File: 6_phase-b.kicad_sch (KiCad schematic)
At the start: 28 parts, among them Q401 BSC072N08NS5, Q402 BSC072N08NS5, U401 IR2181S, U402 AD8418

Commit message: feat: LED routing, encoder interface, footprint updates
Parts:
- removed H?: Pad, symbol Mechanical:MountingHole_Pad
- added H?: Pad, symbol Mechanical:MountingHole_Pad
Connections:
- net at R410.4: now also H?.1

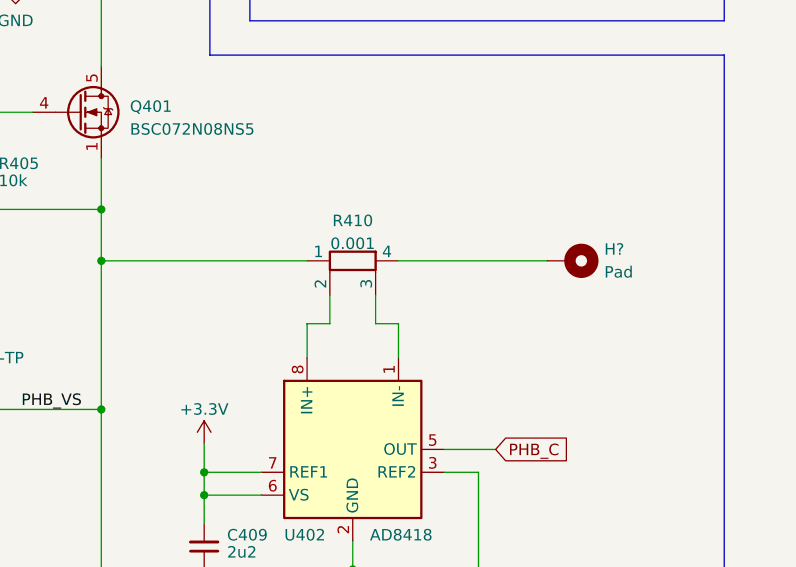
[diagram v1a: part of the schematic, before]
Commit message: feat: footprint assignment, circuit check and routing kickoff
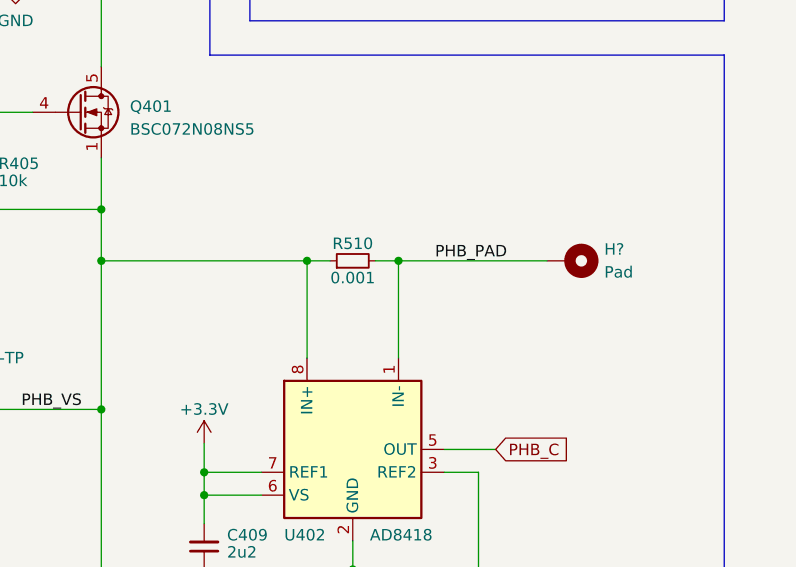
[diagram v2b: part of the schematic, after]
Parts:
- removed R410: 0.001, Resistor_SMD:R_2512_6332Metric, symbol Device:R_Shunt
- added R510: 0.001, Resistor_SMD:R_1206_3216Metric_Pad1.30x1.75mm_HandSolder, symbol Device:R_Small
- C410: footprint Capacitor_SMD:C_0402_1005Metric_Pad0.74x0.62mm_HandSolder -> Capacitor_SMD:C_0603_1608Metric_Pad1.08x0.95mm_HandSolder
- D401: Link (none) -> https://www.digikey.de/en/products/detail/rohm-semiconducto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
- D402: Link (none) -> https://www.digikey.de/en/products/detail/micro-commercial-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
- H?: footprint (none) -> TestPoint:TestPoint_THTPad_4.0x4.0mm_Drill2.0mm
- Q401, Q402: Link (none) -> https://www.digikey.de/en/products/detail/infineon-technolo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
- R408, R409: footprint Resistor_SMD:R_0402_1005Metric_Pad0.72x0.64mm_HandSolder -> Resistor_SMD:R_0603_1608Metric_Pad0.98x0.95mm_HandSolder
- U402: Link (none) -> https://www.digikey.de/en/products/detail/analog-devices-in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
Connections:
- net PHB_VS: now also U402.8 (IN+), R510.1
- net PHB_PAD: now reaches U402.1 (IN-)
- net PHB_PAD: now also H?.1, R510.2
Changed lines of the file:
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@@
   (title_block
     (title "3-Phase Bridge - Phase B")
-    (date "2023-11-25")
+    (date "2023-11-26")
     (rev "1.0")
   )
+  (junction (at 244.475 83.185) (diameter 0) (color 0 0 0 0)
+  )
   (junction (at 189.865 99.695) (diameter 0) (color 0 0 0 0)
   )
@@
   (junction (at 250.19 35.56) (diameter 0) (color 0 0 0 0)
   )
+  (junction (at 234.315 83.185) (diameter 0) (color 0 0 0 0)
+  )
   (junction (at 198.755 66.675) (diameter 0) (color 0 0 0 0)
   )
@@
   (junction (at 201.93 40.005) (diameter 0) (color 0 0 0 0)
   )
-  (wire (pts (xy 236.855 90.17) (xy 236.855 86.995))
-    (stroke (width 0) (type default))
-  )
   (wire (pts (xy 42.545 95.885) (xy 47.625 95.885))
     (stroke (width 0) (type default))
@@
     (stroke (width 0) (type default))
   )
-  (wire (pts (xy 241.935 86.995) (xy 241.935 90.17))
-    (stroke (width 0) (type default))
-  )
   (wire (pts (xy 191.77 48.895) (xy 191.77 52.07))
     (stroke (width 0) (type default))
@@
     (stroke (width 0) (type default))
   )
-  (wire (pts (xy 241.935 90.17) (xy 244.475 90.17))
-    (stroke (width 0) (type default))
-  )
   (wire (pts (xy 77.47 73.66) (xy 77.47 76.2))
     (stroke (width 0) (type default))
   )
-  (wire (pts (xy 234.315 90.17) (xy 236.855 90.17))
-    (stroke (width 0) (type default))
-  )
   (polyline (pts (xy 223.52 60.325) (xy 223.52 20.955))
     (stroke (width 0) (type default))
@@
     (stroke (width 0) (type default))
   )
-  (wire (pts (xy 234.315 93.98) (xy 234.315 90.17))
+  (wire (pts (xy 234.315 83.185) (xy 234.315 93.98))
     (stroke (width 0) (type default))
   )
@@
     (stroke (width 0) (type default))
   )
+  (wire (pts (xy 244.475 83.185) (xy 260.985 83.185))
+    (stroke (width 0) (type default))
+  )
   (wire (pts (xy 229.235 109.22) (xy 222.885 109.22))
     (stroke (width 0) (type default))
@@
     (stroke (width 0) (type default))
   )
+  (wire (pts (xy 234.315 83.185) (xy 236.855 83.185))
+    (stroke (width 0) (type default))
+  )
   (wire (pts (xy 239.395 117.475) (xy 253.365 117.475))
     (stroke (width 0) (type default))
@@
     (stroke (width 0) (type default))
   )
-  (wire (pts (xy 244.475 83.185) (xy 260.985 83.185))
+  (wire (pts (xy 241.935 83.185) (xy 244.475 83.185))
     (stroke (width 0) (type default))
   )
@@
     (stroke (width 0) (type default))
   )
-  (wire (pts (xy 244.475 90.17) (xy 244.475 93.98))
+  (wire (pts (xy 244.475 83.185) (xy 244.475 93.98))
     (stroke (width 0) (type default))
   )
@@
   (label "PHB_HOUT_G" (at 185.42 66.675 0) (fields_autoplaced)
     (effects (font (size 1.27 1.27)) (justify left bottom))
+  )
+  (label "PHB_PAD" (at 256.54 83.185 180) (fields_autoplaced)
+    (effects (font (size 1.27 1.27)) (justify right bottom))
   )
   (label "PHB_HOUT" (at 108.585 85.725 180) (fields_autoplaced)
@@
     (property "Datasheet" "http://www.infineon.com/dgdl/Infineon-BSC072N08NS5-DS-v02_00-EN.pdf?fileId=5546d4624ad04ef9014ae3d8e8192c7c" (at 208.915 66.675 90)
       (effects (font (size 1.27 1.27)) (justify left) hide)
+    )
+    (property "Link" "https://www.digikey.de/en/products/detail/infineon-technologies/BSC072N08NS5ATMA1/5959908" (at 208.915 66.675 0)
+      (effects (font (size 1.27 1.27)) hide)
     )
     (pin "1")
@@
       (effects (font (size 1.27 1.27)) hide)
     )
+    (property "Link" "https://www.digikey.de/en/products/detail/analog-devices-inc/AD8418AWBRZ/4571735" (at 239.395 104.14 0)
+      (effects (font (size 1.27 1.27)) hide)
+    )
     (pin "1")
     (pin "2")
@@
       (effects (font (size 1.27 1.27)) (justify left))
     )
-    (property "Footprint" "Resistor_SMD:R_0402_1005Metric_Pad0.72x0.64mm_HandSolder" (at 184.785 105.41 0)
+    (property "Footprint" "Resistor_SMD:R_0603_1608Metric_Pad0.98x0.95mm_HandSolder" (at 184.785 105.41 0)
       (effects (font (size 1.27 1.27)) hide)
     )
@@
         (path "/9dea2e18-5867-4ed4-a12d-7ee109225de0/912dc4da-f7bc-46bd-8800-06fc31d708dd"
           (reference "#PWR044") (unit 1)
-        )
-      )
-    )
-  )
-  (symbol (lib_id "Device:R_Shunt") (at 239.395 83.185 90) (mirror x) (unit 1)
-    (in_bom yes) (on_board yes) (dnp no)
-    (property "Reference" "R410" (at 239.395 78.74 90)
-      (effects (font (size 1.27 1.27)))
-    )
-    (property "Value" "0.001" (at 239.395 81.28 90)
-      (effects (font (size 1.27 1.27)))
-    )
-    (property "Footprint" "Resistor_SMD:R_2512_6332Metric" (at 239.395 81.407 90)
-      (effects (font (size 1.27 1.27)) hide)
-    )
-    (property "Datasheet" "~" (at 239.395 83.185 0)
-      (effects (font (size 1.27 1.27)) hide)
-    )
-    (property "Link" "https://www.digikey.de/en/products/detail/bourns-inc/CSS2H-2512R-1L00F/6023764" (at 239.395 83.185 90)
-      (effects (font (size 1.27 1.27)) hide)
-    )
-    (pin "1")
-    (pin "2")
-    (pin "3")
-    (pin "4")
-    (instances
-      (project "ESC_R1"
-        (path "/9dea2e18-5867-4ed4-a12d-7ee109225de0/a82201a8-9dca-4a1d-828e-2de3fb3c1adb"
-          (reference "R410") (unit 1)
-        )
-        (path "/9dea2e18-5867-4ed4-a12d-7ee109225de0/c42edb1a-90dc-4d64-9c27-05abb4553a36"
-          (reference "R610") (unit 1)
-        )
-        (path "/9dea2e18-5867-4ed4-a12d-7ee109225de0/912dc4da-f7bc-46bd-8800-06fc31d708dd"
-          (reference "R23") (unit 1)
         )
       )
@@
       (effects (font (size 1.27 1.27)) (justify left) hide)
     )
+    (property "Link" "https://www.digikey.de/en/products/detail/infineon-technologies/BSC072N08NS5ATMA1/5959908" (at 208.915 133.35 0)
+      (effects (font (size 1.27 1.27)) hide)
+    )
     (pin "1")
     (pin "2")
@@
       (effects (font (size 1.27 1.27)) hide)
     )
+    (property "Link" "https://www.digikey.de/en/products/detail/micro-commercial-co/MBR0530-TP/717251" (at 189.865 92.71 0)
+      (effects (font (size 1.27 1.27)) hide)
+    )
     (pin "1")
     (pin "2")
@@
         )
         (path "/9dea2e18-5867-4ed4-a12d-7ee109225de0/c42edb1a-90dc-4d64-9c27-05abb4553a36"
-          (reference "D3") (unit 1)
+          (reference "D602") (unit 1)
         )
         (path "/9dea2e18-5867-4ed4-a12d-7ee109225de0/912dc4da-f7bc-46bd-8800-06fc31d708dd"
@@
       (effects (font (size 1.27 1.27)) hide)
     )
+    (property "Link" "https://www.digikey.de/en/products/detail/rohm-semiconductor/RB162MM-60TR/5001869" (at 114.935 74.295 0)
+      (effects (font (size 1.27 1.27)) hide)
+    )
     (pin "1")
     (pin "2")
@@
     )
   )
+  (symbol (lib_id "Device:R_Small") (at 239.395 83.185 90) (unit 1)
+    (in_bom yes) (on_board yes) (dnp no)
+    (property "Reference" "R510" (at 239.395 81.28 90)
+      (effects (font (size 1.27 1.27)))
+    )
+    (property "Value" "0.001" (at 239.395 85.09 90)
+      (effects (font (size 1.27 1.27)))
+    )
+    (property "Footprint" "Resistor_SMD:R_1206_3216Metric_Pad1.30x1.75mm_HandSolder" (at 239.395 83.185 0)
+      (effects (font (size 1.27 1.27)) hide)
+    )
+    (property "Datasheet" "~" (at 239.395 83.185 0)
+      (effects (font (size 1.27 1.27)) hide)
+    )
+    (pin "1")
+    (pin "2")
+    (instances
+      (project "ESC_R1"
+        (path "/9dea2e18-5867-4ed4-a12d-7ee109225de0/a82201a8-9dca-4a1d-828e-2de3fb3c1adb"
+          (reference "R510") (unit 1)
+        )
+        (path "/9dea2e18-5867-4ed4-a12d-7ee109225de0/c42edb1a-90dc-4d64-9c27-05abb4553a36"
+          (reference "R610") (unit 1)
+        )
+      )
+    )
+  )
   (symbol (lib_id "Device:R_Small") (at 259.08 35.56 90) (unit 1)
     (in_bom yes) (on_board yes) (dnp no)
@@
       (effects (font (size 1.27 1.27)) (justify left))
     )
-    (property "Footprint" "" (at 263.525 83.185 0)
+    (property "Footprint" "TestPoint:TestPoint_THTPad_4.0x4.0mm_Drill2.0mm" (at 263.525 83.185 0)
       (effects (font (size 1.27 1.27)) hide)
     )
@@
       (effects (font (size 1.27 1.27)))
     )
-    (property "Footprint" "Resistor_SMD:R_0402_1005Metric_Pad0.72x0.64mm_HandSolder" (at 196.85 99.695 0)
+    (property "Footprint" "Resistor_SMD:R_0603_1608Metric_Pad0.98x0.95mm_HandSolder" (at 196.85 99.695 0)
       (effects (font (size 1.27 1.27)) hide)
     )
@@
       (effects (font (size 1.27 1.27)) (justify right))
     )
-    (property "Footprint" "Capacitor_SMD:C_0402_1005Metric_Pad0.74x0.62mm_HandSolder" (at 250.19 41.275 0)
-      (effects (font (size 1.27 1.27)) hide)
-    )
+    (property "Footprint" "Capacitor_SMD:C_0603_1608Metric_Pad1.08x0.95mm_HandSolder" (at 250.19 41.275 0)
+      (effects (font (size 1.27 1.27)) hide)
+    )

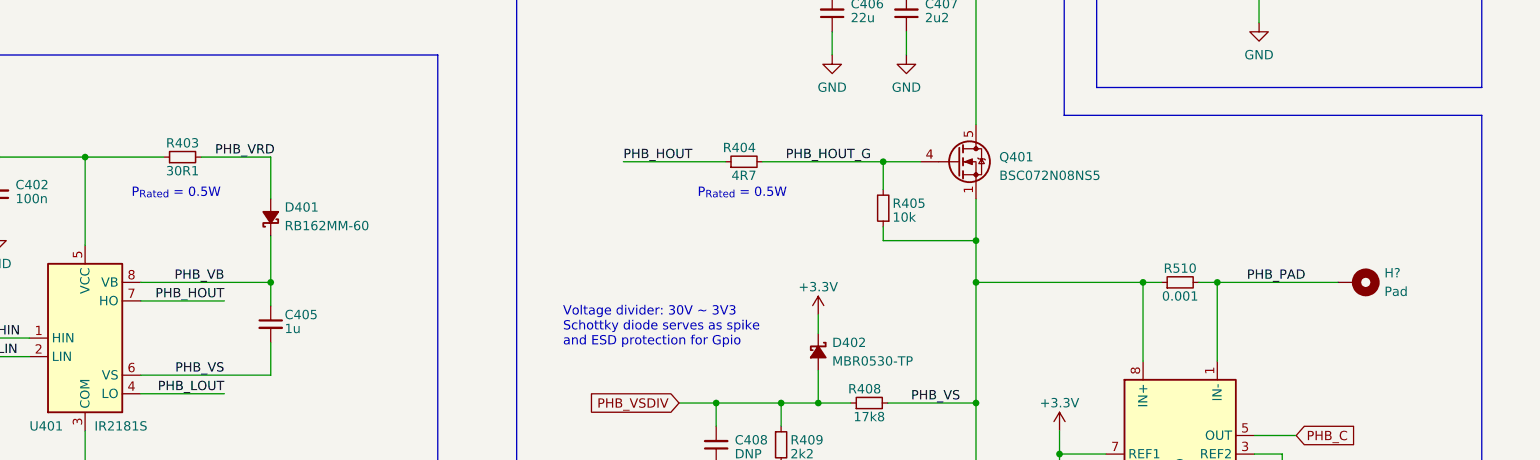
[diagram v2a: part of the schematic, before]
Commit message: fix: fixed LTSpice simulation and updated track widths accordingly
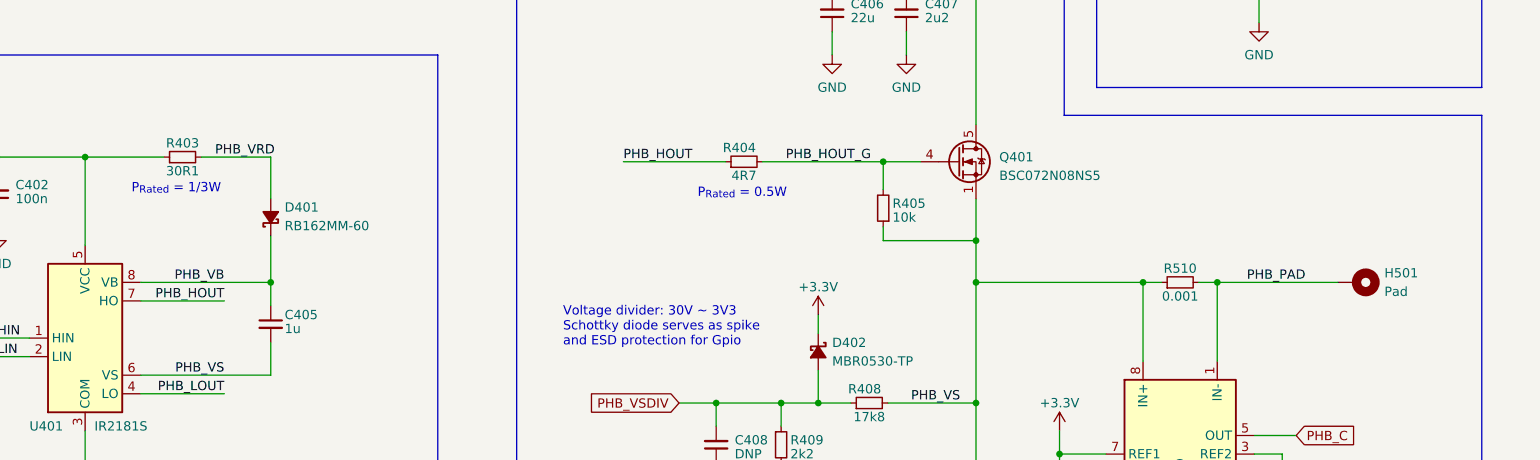
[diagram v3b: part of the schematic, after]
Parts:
- removed H?: Pad, TestPoint:TestPoint_THTPad_4.0x4.0mm_Drill2.0mm, symbol Mechanical:MountingHole_Pad
- added H501: Pad, TestPoint:TestPoint_Pad_5.0x7.0mm, symbol Mechanical:MountingHole_Pad
- R403: Link (none) -> https://www.digikey.de/en/products/detail/vishay-dale/CRCW0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
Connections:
- net PHB_PAD: now also H501.1
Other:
- note added: "P_{Rated} = 1/3W"
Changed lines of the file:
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@@
     (effects (font (size 1.6 1.6) italic) (justify left bottom))
   )
-  (text "P_{Rated} = 0.5W\n" (at 95.885 71.755 0)
+  (text "P_{Rated} = 1/3W\n" (at 95.885 71.12 0)
     (effects (font (size 1.27 1.27)) (justify left bottom))
   )
@@
       (effects (font (size 1.27 1.27)) hide)
     )
+    (property "Link" "https://www.digikey.de/en/products/detail/vishay-dale/CRCW060333R0FKEAHP/2222237" (at 102.87 66.04 0)
+      (effects (font (size 1.27 1.27)) hide)
+    )
     (pin "1")
     (pin "2")
@@
     )
   )
+  (symbol (lib_id "Mechanical:MountingHole_Pad") (at 263.525 83.185 270) (unit 1)
+    (in_bom yes) (on_board yes) (dnp no)
+    (property "Reference" "H501" (at 267.335 81.9149 90)
+      (effects (font (size 1.27 1.27)) (justify left))
+    )
+    (property "Value" "Pad" (at 267.335 84.455 90)
+      (effects (font (size 1.27 1.27)) (justify left))
+    )
+    (property "Footprint" "TestPoint:TestPoint_Pad_5.0x7.0mm" (at 263.525 83.185 0)
+      (effects (font (size 1.27 1.27)) hide)
+    )
+    (property "Datasheet" "~" (at 263.525 83.185 0)
+      (effects (font (size 1.27 1.27)) hide)
+    )
+    (pin "1")
+    (instances
+      (project "ESC_R1"
+        (path "/9dea2e18-5867-4ed4-a12d-7ee109225de0/a82201a8-9dca-4a1d-828e-2de3fb3c1adb"
+          (reference "H501") (unit 1)
+        )
+        (path "/9dea2e18-5867-4ed4-a12d-7ee109225de0/c42edb1a-90dc-4d64-9c27-05abb4553a36"
+          (reference "H601") (unit 1)
+        )
+      )
+    )
+  )
   (symbol (lib_id "Device:D_Schottky_Small_Filled") (at 114.935 74.295 90) (unit 1)
     (in_bom yes) (on_board yes) (dnp no)
@@
         )
       )
-    )
-  )
-  (symbol (lib_id "Mechanical:MountingHole_Pad") (at 263.525 83.185 270) (unit 1)
-    (in_bom yes) (on_board yes) (dnp no)
-    (property "Reference" "H?" (at 267.335 81.9149 90)
-      (effects (font (size 1.27 1.27)) (justify left))
-    )
-    (property "Value" "Pad" (at 267.335 84.455 90)
-      (effects (font (size 1.27 1.27)) (justify left))
-    )
-    (property "Footprint" "TestPoint:TestPoint_THTPad_4.0x4.0mm_Drill2.0mm" (at 263.525 83.185 0)
-      (effects (font (size 1.27 1.27)) hide)
-    )
-    (property "Datasheet" "~" (at 263.525 83.185 0)
-      (effects (font (size 1.27 1.27)) hide)
-    )
-    (pin "1")
-    (instances
-      (project "ESC_R1"
-        (path "/9dea2e18-5867-4ed4-a12d-7ee109225de0/a82201a8-9dca-4a1d-828e-2de3fb3c1adb"
-          (reference "H?") (unit 1)
-        )
-        (path "/9dea2e18-5867-4ed4-a12d-7ee109225de0/c42edb1a-90dc-4d64-9c27-05abb4553a36"
-          (reference "H601") (unit 1)
-        )
-        (path "/9dea2e18-5867-4ed4-a12d-7ee109225de0/912dc4da-f7bc-46bd-8800-06fc31d708dd"
-          (reference "H2") (unit 1)
-        )
-      )
